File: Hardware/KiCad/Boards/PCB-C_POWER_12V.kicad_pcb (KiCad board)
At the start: 2 copper layers, 130 x 94 mm, 0 parts

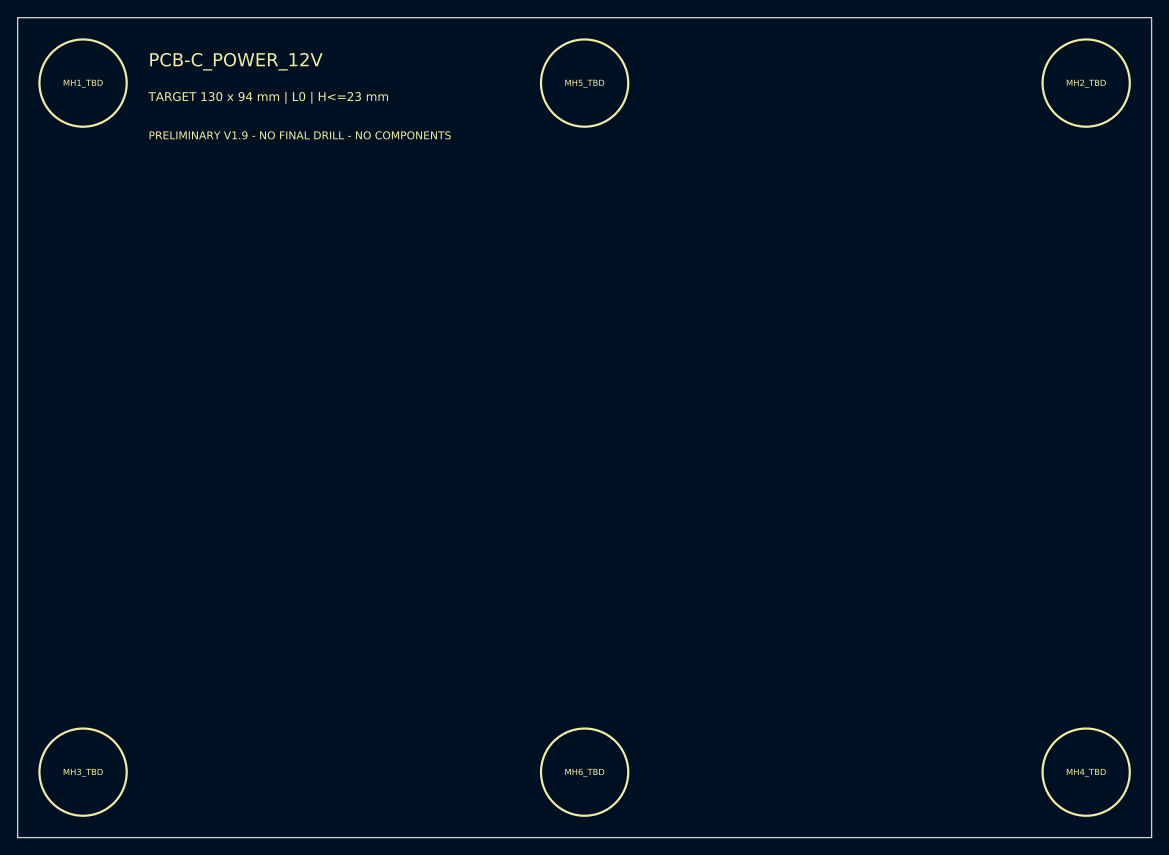
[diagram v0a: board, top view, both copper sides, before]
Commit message: hardware: add PCB-C functional and height placeholders
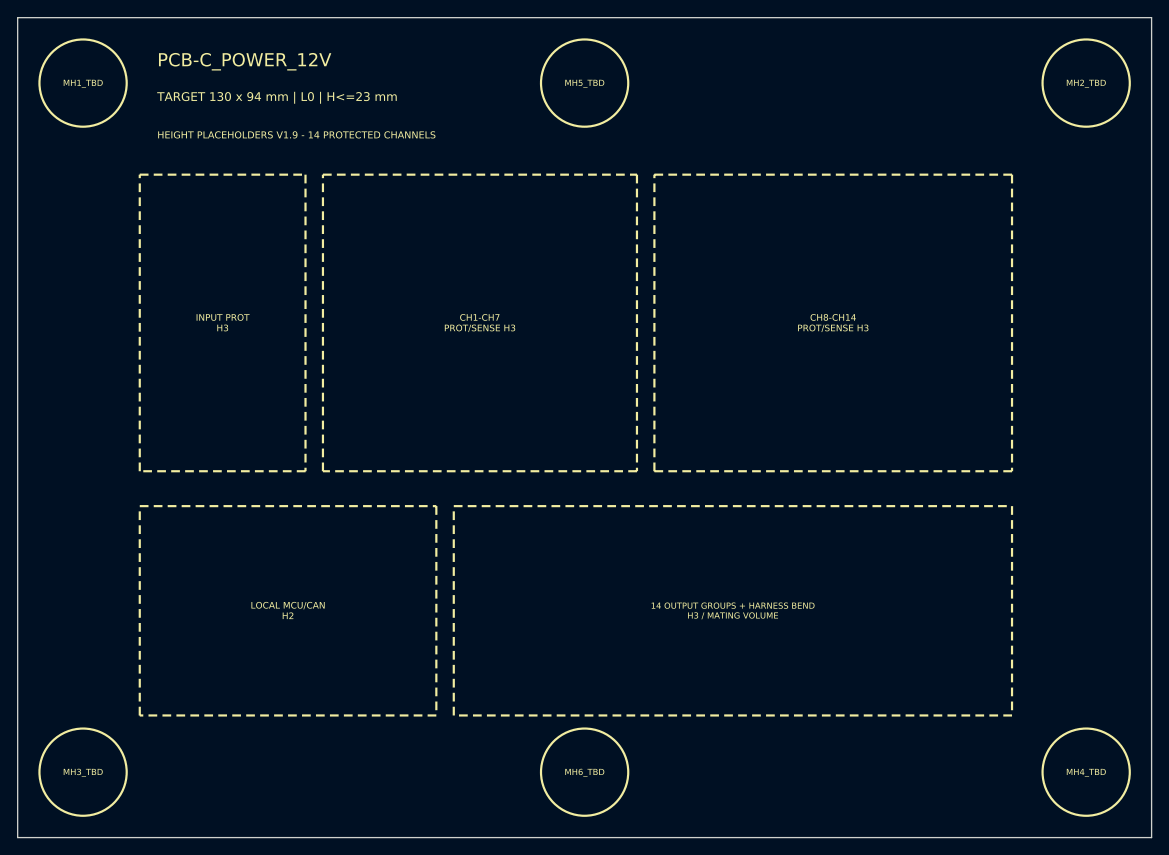
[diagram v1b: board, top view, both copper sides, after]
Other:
- board text added: "14 OUTPUT GROUPS + HARNESS BEND H3 / MATING VOLUME"
- board text added: "CH1-CH7 PROT/SENSE H3"
- board text added: "CH8-CH14 PROT/SENSE H3"
- board text added: "HEIGHT PLACEHOLDERS V1.9 - 14 PROTECTED CHANNELS"
- board text added: "INPUT PROT H3"
- board text added: "LOCAL MCU/CAN H2"
- board text removed: "PRELIMINARY V1.9 - NO FINAL DRILL - NO COMPONENTS"
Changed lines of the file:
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@@
 		(pad_to_mask_clearance 0)
 		(allow_soldermask_bridges_in_footprints no)
-		(tenting
-			(front yes)
-			(back yes)
-		)
-		(covering
-			(front no)
-			(back no)
-		)
-		(plugging
-			(front no)
-			(back no)
-		)
-		(capping no)
-		(filling no)
-		(pcbplotparams
-			(layerselection 0x00000000_00000000_55555555_5755f5ff)
-			(plot_on_all_layers_selection 0x00000000_00000000_00000000_00000000)
-			(disableapertmacros no)
-			(usegerberextensions no)
-			(usegerberattributes yes)
-			(usegerberadvancedattributes yes)
-			(creategerberjobfile yes)
-			(dashed_line_dash_ratio 12)
-			(dashed_line_gap_ratio 3)
-			(svgprecision 4)
-			(plotframeref no)
-			(mode 1)
-			(useauxorigin no)
-			(pdf_front_fp_property_popups yes)
-			(pdf_back_fp_property_popups yes)
-			(pdf_metadata yes)
-			(pdf_single_document no)
-			(dxfpolygonmode yes)
-			(dxfimperialunits yes)
-			(dxfusepcbnewfont yes)
-			(psnegative no)
-			(psa4output no)
-			(plot_black_and_white yes)
-			(sketchpadsonfab no)
-			(plotpadnumbers no)
-			(hidednponfab no)
-			(sketchdnponfab yes)
-			(crossoutdnponfab yes)
-			(subtractmaskfromsilk no)
-			(outputformat 1)
-			(mirror no)
-			(drillshape 1)
-			(scaleselection 1)
-			(outputdirectory "")
-		)
 	)
-	(gr_circle
-		(center 27.5 27.5)
-		(end 32.5 27.5)
-		(stroke
-			(width 0.25)
-			(type dash)
-		)
-		(fill no)
-		(layer "F.SilkS")
-	)
-	(gr_circle
-		(center 27.5 106.5)
-		(end 32.5 106.5)
-		(stroke
-			(width 0.25)
-			(type dash)
-		)
-		(fill no)
-		(layer "F.SilkS")
-	)
-	(gr_circle
-		(center 85 27.5)
-		(end 90 27.5)
-		(stroke
-			(width 0.25)
-			(type dash)
-		)
-		(fill no)
-		(layer "F.SilkS")
-	)
-	(gr_circle
-		(center 85 106.5)
-		(end 90 106.5)
-		(stroke
-			(width 0.25)
-			(type dash)
-		)
-		(fill no)
-		(layer "F.SilkS")
-	)
-	(gr_circle
-		(center 142.5 27.5)
-		(end 147.5 27.5)
-		(stroke
-			(width 0.25)
-			(type dash)
-		)
-		(fill no)
-		(layer "F.SilkS")
-	)
-	(gr_circle
-		(center 142.5 106.5)
-		(end 147.5 106.5)
-		(stroke
-			(width 0.25)
-			(type dash)
-		)
-		(fill no)
-		(layer "F.SilkS")
-	)
-	(gr_rect
-		(start 20 20)
-		(end 150 114)
-		(stroke
-			(width 0.05)
-			(type default)
-		)
-		(fill no)
-		(layer "Edge.Cuts")
-	)
-	(gr_text "MH1_TBD"
-		(at 27.5 27.5 0)
-		(layer "F.SilkS")
-		(effects
-			(font
-				(size 0.7 0.7)
-				(thickness 0.14)
-			)
-		)
-	)
-	(gr_text "MH3_TBD"
-		(at 27.5 106.5 0)
-		(layer "F.SilkS")
-		(effects
-			(font
-				(size 0.7 0.7)
-				(thickness 0.14)
-			)
-		)
-	)
-	(gr_text "MH5_TBD"
-		(at 85 27.5 0)
-		(layer "F.SilkS")
-		(effects
-			(font
-				(size 0.7 0.7)
-				(thickness 0.14)
-			)
-		)
-	)
-	(gr_text "MH6_TBD"
-		(at 85 106.5 0)
-		(layer "F.SilkS")
-		(effects
-			(font
-				(size 0.7 0.7)
-				(thickness 0.14)
-			)
-		)
-	)
-	(gr_text "MH2_TBD"
-		(at 142.5 27.5 0)
-		(layer "F.SilkS")
-		(effects
-			(font
-				(size 0.7 0.7)
-				(thickness 0.14)
-			)
-		)
-	)
-	(gr_text "MH4_TBD"
-		(at 142.5 106.5 0)
-		(layer "F.SilkS")
-		(effects
-			(font
-				(size 0.7 0.7)
-				(thickness 0.14)
-			)
-		)
-	)
-	(gr_text "PRELIMINARY V1.9 - NO FINAL DRILL - NO COMPONENTS"
-		(at 35 33 0)
-		(layer "F.SilkS")
-		(effects
-			(font
-				(size 0.9 0.9)
-				(thickness 0.18)
-			)
-			(justify left top)
-		)
-	)
-	(gr_text "TARGET 130 x 94 mm | L0 | H<=23 mm"
-		(at 35 28.5 0)
-		(layer "F.SilkS")
-		(effects
-			(font
-				(size 1 1)
-				(thickness 0.2)
-			)
-			(justify left top)
-		)
-	)
-	(gr_text "PCB-C_POWER_12V"
-		(at 35 24 0)
-		(layer "F.SilkS")
-		(effects
-			(font
-				(size 1.5 1.5)
-				(thickness 0.3)
-			)
-			(justify left top)
-		)
-	)
+	(gr_rect (start 20 20) (end 150 114) (stroke (width 0.05) (type default)) (fill no) (layer "Edge.Cuts"))
+	(gr_text "PCB-C_POWER_12V" (at 36 24 0) (layer "F.SilkS") (effects (font (size 1.5 1.5) (thickness 0.3)) (justify left top)))
+	(gr_text "TARGET 130 x 94 mm | L0 | H<=23 mm" (at 36 28.5 0) (layer "F.SilkS") (effects (font (size 1 1) (thickness 0.2)) (justify left top)))
+	(gr_text "HEIGHT PLACEHOLDERS V1.9 - 14 PROTECTED CHANNELS" (at 36 33 0) (layer "F.SilkS") (effects (font (size 0.8 0.8) (thickness 0.16)) (justify left top)))
+	(gr_circle (center 27.5 27.5) (end 32.5 27.5) (stroke (width 0.25) (type dash)) (fill no) (layer "F.SilkS"))
+	(gr_circle (center 27.5 106.5) (end 32.5 106.5) (stroke (width 0.25) (type dash)) (fill no) (layer "F.SilkS"))
+	(gr_circle (center 85 27.5) (end 90 27.5) (stroke (width 0.25) (type dash)) (fill no) (layer "F.SilkS"))
+	(gr_circle (center 85 106.5) (end 90 106.5) (stroke (width 0.25) (type dash)) (fill no) (layer "F.SilkS"))
+	(gr_circle (center 142.5 27.5) (end 147.5 27.5) (stroke (width 0.25) (type dash)) (fill no) (layer "F.SilkS"))
+	(gr_circle (center 142.5 106.5) (end 147.5 106.5) (stroke (width 0.25) (type dash)) (fill no) (layer "F.SilkS"))
+	(gr_text "MH1_TBD" (at 27.5 27.5 0) (layer "F.SilkS") (effects (font (size 0.7 0.7) (thickness 0.14))))
+	(gr_text "MH2_TBD" (at 142.5 27.5 0) (layer "F.SilkS") (effects (font (size 0.7 0.7) (thickness 0.14))))
+	(gr_text "MH3_TBD" (at 27.5 106.5 0) (layer "F.SilkS") (effects (font (size 0.7 0.7) (thickness 0.14))))
+	(gr_text "MH4_TBD" (at 142.5 106.5 0) (layer "F.SilkS") (effects (font (size 0.7 0.7) (thickness 0.14))))
+	(gr_text "MH5_TBD" (at 85 27.5 0) (layer "F.SilkS") (effects (font (size 0.7 0.7) (thickness 0.14))))
+	(gr_text "MH6_TBD" (at 85 106.5 0) (layer "F.SilkS") (effects (font (size 0.7 0.7) (thickness 0.14))))
+	(gr_rect (start 34 38) (end 53 72) (stroke (width 0.25) (type dash)) (fill no) (layer "F.SilkS"))
+	(gr_text "INPUT PROT\nH3" (at 43.5 55 0) (layer "F.SilkS") (effects (font (size 0.75 0.75) (thickness 0.14))))
+	(gr_rect (start 55 38) (end 91 72) (stroke (width 0.25) (type dash)) (fill no) (layer "F.SilkS"))
+	(gr_text "CH1-CH7\nPROT/SENSE H3" (at 73 55 0) (layer "F.SilkS") (effects (font (size 0.75 0.75) (thickness 0.14))))
+	(gr_rect (start 93 38) (end 134 72) (stroke (width 0.25) (type dash)) (fill no) (layer "F.SilkS"))
+	(gr_text "CH8-CH14\nPROT/SENSE H3" (at 113.5 55 0) (layer "F.SilkS") (effects (font (size 0.75 0.75) (thickness 0.14))))
+	(gr_rect (start 34 76) (end 68 100) (stroke (width 0.25) (type dash)) (fill no) (layer "F.SilkS"))
+	(gr_text "LOCAL MCU/CAN\nH2" (at 51 88 0) (layer "F.SilkS") (effects (font (size 0.75 0.75) (thickness 0.14))))
+	(gr_rect (start 70 76) (end 134 100) (stroke (width 0.25) (type dash)) (fill no) (layer "F.SilkS"))
+	(gr_text "14 OUTPUT GROUPS + HARNESS BEND\nH3 / MATING VOLUME" (at 102 88 0) (layer "F.SilkS") (effects (font (size 0.7 0.7) (thickness 0.13))))
+	(gr_rect (start 68 74) (end 136 102) (stroke (width 0.3) (type dash)) (fill no) (layer "Margin"))
 	(embedded_fonts no)
 )
